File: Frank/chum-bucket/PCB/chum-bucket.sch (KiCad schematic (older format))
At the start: 3 parts

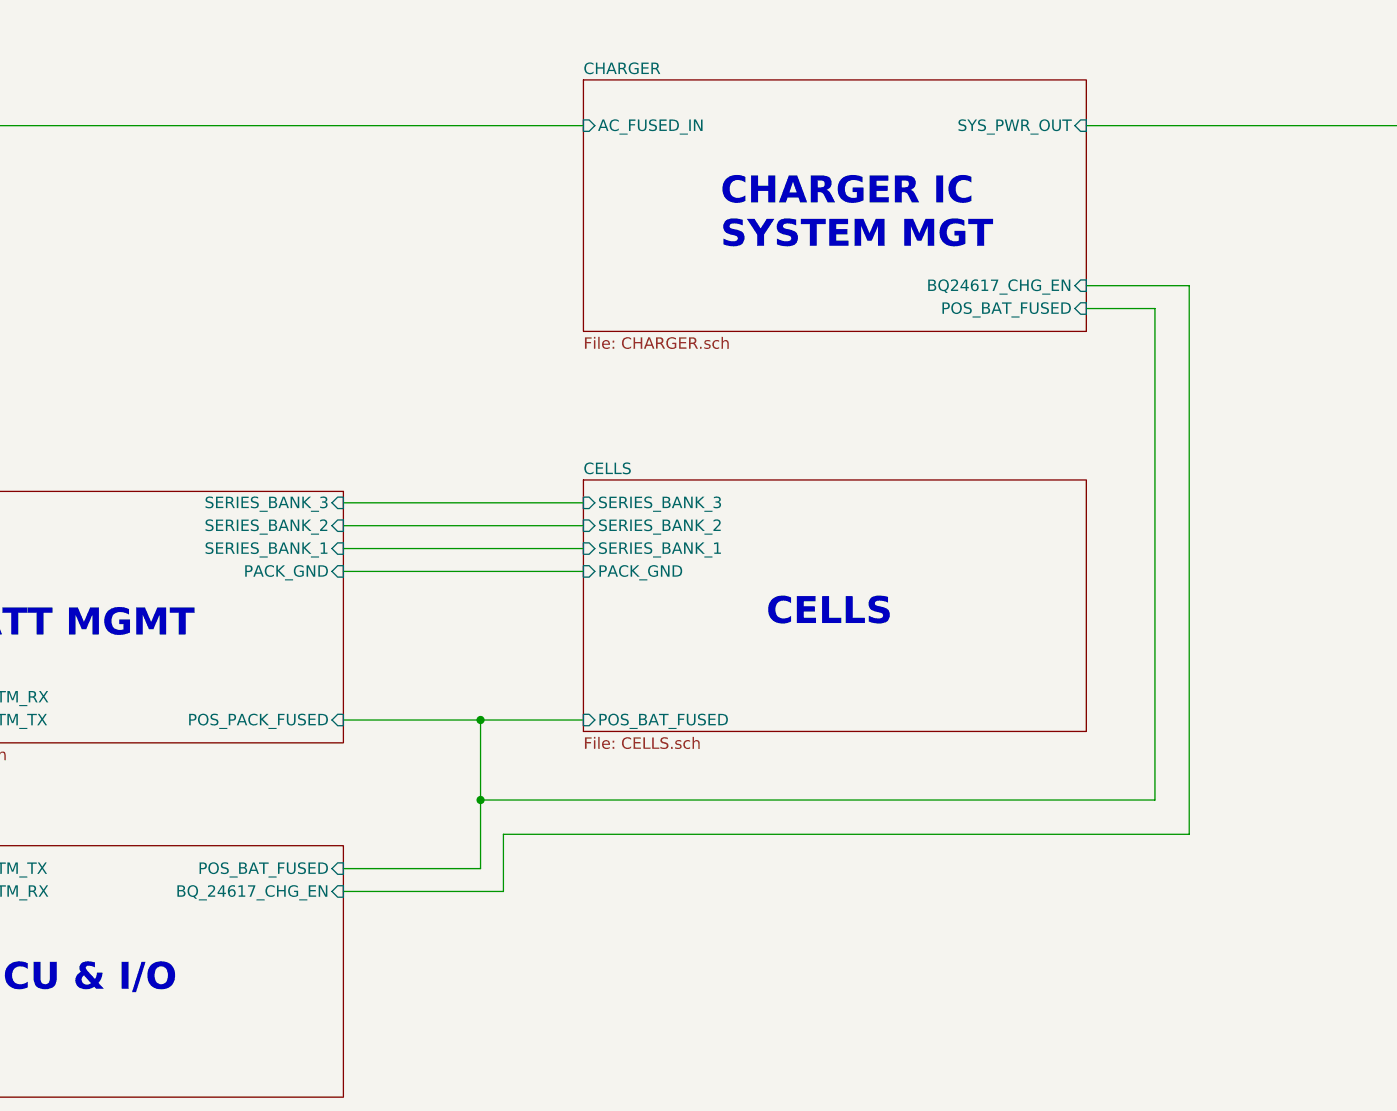
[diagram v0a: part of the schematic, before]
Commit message: minor schematic update + inrush sim
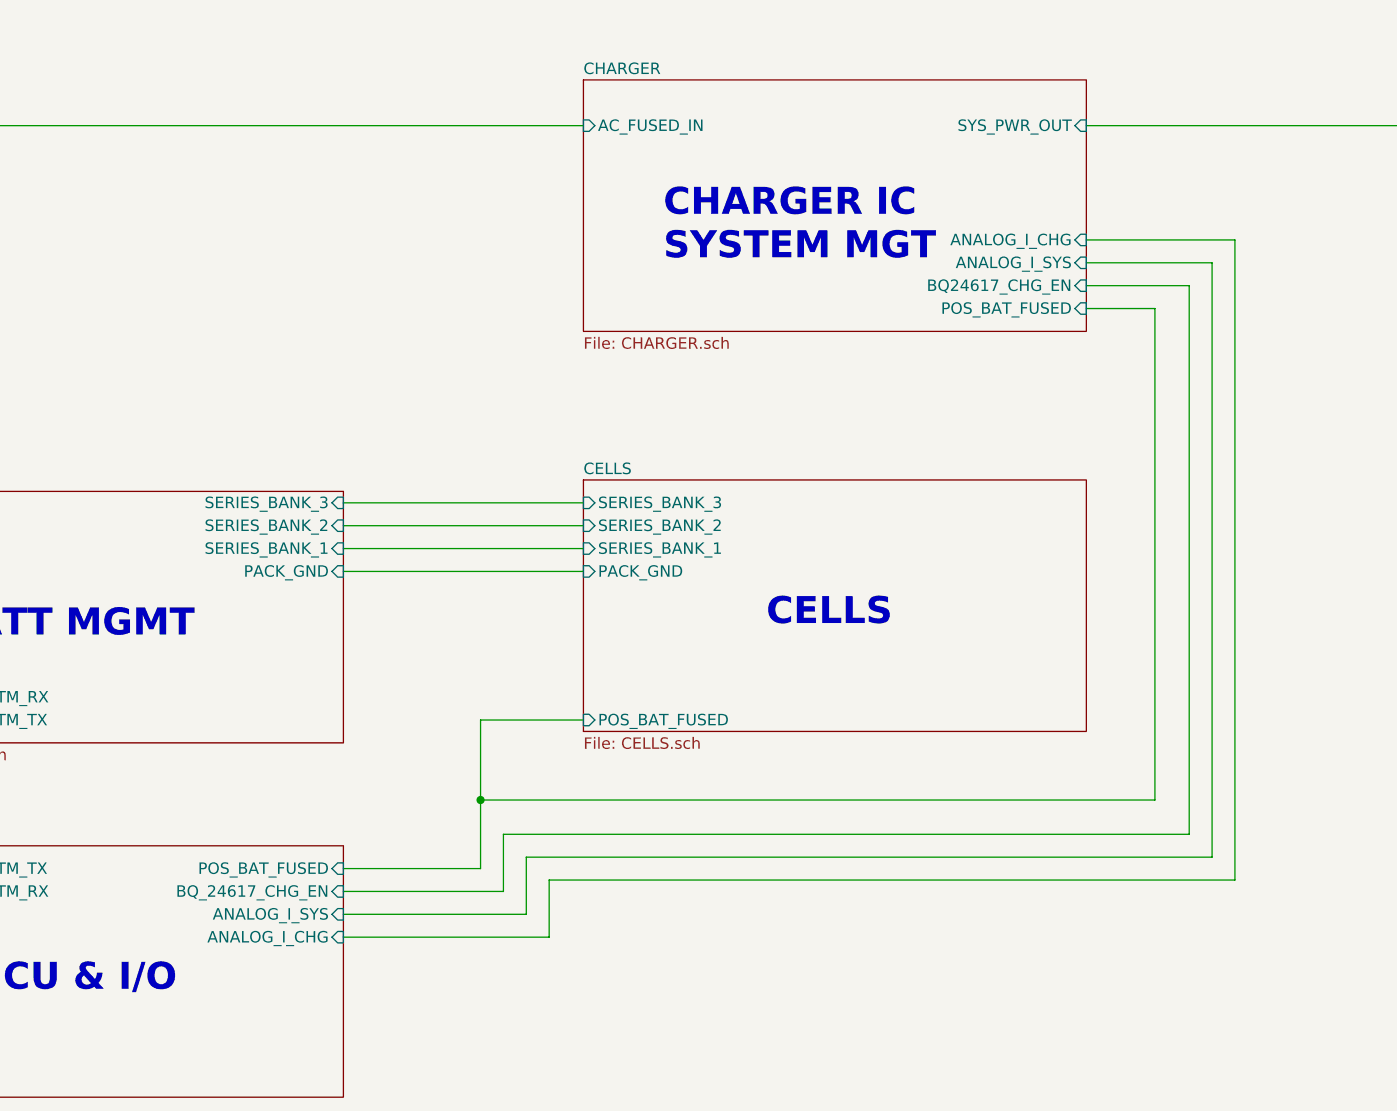
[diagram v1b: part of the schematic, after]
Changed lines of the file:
@@
 F6 "UART_BQ79606_STM_TX" I L 1550 5800 50
 F7 "UART_BQ79606_STM_RX" I L 1550 5900 50
+F8 "ANALOG_I_SYS" I R 3750 6000 50
+F9 "ANALOG_I_CHG" I R 3750 6100 50
 $EndSheet
 Text Notes 5600 4750 0    118  ~ 24
@@
 F6 "SERIES_BANK_3" I L 4800 4200 50
 $EndSheet
-Text Notes 5400 3100 0    118  ~ 24
+Text Notes 5150 3150 0    118  ~ 24
 CHARGER IC\nSYSTEM MGT
 $Sheet
@@
 F4 "SYS_PWR_OUT" I R 7000 2550 50
 F5 "POS_BAT_FUSED" I R 7000 3350 50
+F6 "ANALOG_I_SYS" I R 7000 3150 50
+F7 "ANALOG_I_CHG" I R 7000 3050 50
 $EndSheet
 $Sheet
@@
 F2 "~BQ79606_FAULT" I L 1550 4950 50
 F3 "BQ79606_WAKE" I L 1550 4850 50
-F4 "POS_PACK_FUSED" I R 3750 5150 50
-F5 "SERIES_BANK_3" I R 3750 4200 50
-F6 "SERIES_BANK_2" I R 3750 4300 50
-F7 "SERIES_BANK_1" I R 3750 4400 50
-F8 "PACK_GND" I R 3750 4500 50
-F9 "UART_BQ79606_STM_RX" I L 1550 5050 50
-F10 "UART_BQ79606_STM_TX" I L 1550 5150 50
+F4 "SERIES_BANK_3" I R 3750 4200 50
+F5 "SERIES_BANK_2" I R 3750 4300 50
+F6 "SERIES_BANK_1" I R 3750 4400 50
+F7 "PACK_GND" I R 3750 4500 50
+F8 "UART_BQ79606_STM_RX" I L 1550 5050 50
+F9 "UART_BQ79606_STM_TX" I L 1550 5150 50
 $EndSheet
 Text Notes 3100 4800 2    118  ~ 24
@@
 	4350 5800 4350 5500
 Wire Wire Line
-	3750 5150 4350 5150
-Wire Wire Line
 	4350 5500 4350 5150
 Connection ~ 4350 5500
-Connection ~ 4350 5150
 Wire Wire Line
 	4350 5150 4800 5150
@@
 Wire Wire Line
 	7450 3250 7000 3250
+Wire Wire Line
+	3750 6000 4550 6000
+Wire Wire Line
+	4550 6000 4550 5750
+Wire Wire Line
+	4550 5750 7550 5750
+Wire Wire Line
+	7550 5750 7550 3150
+Wire Wire Line
+	7550 3150 7000 3150
+Wire Wire Line
+	3750 6100 4650 6100
+Wire Wire Line
+	4650 6100 4650 5850
+Wire Wire Line
+	4650 5850 7650 5850
+Wire Wire Line
+	7650 5850 7650 3050
+Wire Wire Line
+	7650 3050 7000 3050
 $EndSCHEMATC

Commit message: Weekends work. Final component selection then ready for review :)
huge oof
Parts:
- removed F?: Fuse, symbol Device:Fuse
- removed J?: XT-30 RA, symbol Connector_Generic:Conn_01x02
- added J?: WPT_CONN, symbol Connector_Generic:Conn_01x02
- added J?: SYS_PWR, symbol Connector_Generic:Conn_01x02
- added J?: ESC_PWR, symbol Connector_Generic:Conn_01x02
- J?: value Conn_01x02 -> AC_ADPTR
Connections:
- net CHARGER/AC_FUSED_IN: now also J?.2 (Pin_2), J?.2 (Pin_2)
- net GND: now also J?.1 (Pin_1), J?.1 (Pin_1), J?.1 (Pin_1)
- new net SYS_MGMT/ESC_PWR_OUT: J?.2 (Pin_2)
- new net SYS_MGMT/SYS_PWR_OUT_PROT: J?.2 (Pin_2)
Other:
- note added: "- 1kW peak power delievery\n- e-fused I/O for decreased footprint\n- Power telemetry delievered via CAN"
- note added: "- 3s8p Lithium cell holders\n- 2A Balancing Current\n- 8A cell charger"
- note added: "CHARGER"
- note added: "Highly Integrated, Small Footprint, Managed Lithium Battery"
- note added: "No need to fuse due to use of \nconventionial and e-fuses downstream"
- note added: "SYS MGMT +\nOUTPUT PROT"
- note removed: "- 3s8p Lithium cell holder\n- Blah Blah\n- Item 3\n- Item 4"
- note removed: "- Item 1\n- Item 2\n- Item 3\n- Item 4"
- note removed: "CHARGER IC\nSYSTEM MGT"
- note removed: "Highly Integrated, Small Footprint, Protected Lithium Battery"
- moved on the sheet: J?

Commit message: batt-management sheet updates
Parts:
- added C?: 10nF, symbol Device:C_Small
- added D?: SMBJ26A, Diode_SMD:D_SMB, symbol Device:D_TVS
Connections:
- net CHARGER/AC_FUSED_IN: now also C?.1, D?.1 (A1)
- net GND: now also C?.2, D?.2 (A2)
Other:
- note added: "- 1kW peak power delievery\n- e-fused I/O for decreased footprint\n- Power telemetry broadcasted via CAN"
- note added: "To do: \n- add voltage monitoring for output busses\n- add current monitoring for ESC bus (hall effect sensor?)"
- note removed: "- 1kW peak power delievery\n- e-fused I/O for decreased footprint\n- Power telemetry delievered via CAN"
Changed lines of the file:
@@
 - 3s8p Lithium cell holders\n- 2A Balancing Current\n- 8A cell charger
 Text Notes 6150 1550 0    39   ~ 0
-- 1kW peak power delievery\n- e-fused I/O for decreased footprint\n- Power telemetry delievered via CAN
+- 1kW peak power delievery\n- e-fused I/O for decreased footprint\n- Power telemetry broadcasted via CAN
 Text Notes 7900 3200 0    118  ~ 24
 SYS MGMT +\nOUTPUT PROT
@@
 	-1   0    0    1
 $EndComp
-Text Notes 1400 2100 0    50   ~ 0
+Text Notes 1500 2450 0    50   ~ 0
 No need to fuse due to use of \nconventionial and e-fuses downstream
 Wire Wire Line
@@
 	6850 3350 7550 3350
 Connection ~ 1450 2550
-Wire Wire Line
-	1450 2550 2850 2550
 Wire Wire Line
 	4150 3900 2850 3900
@@
 F10 "ESC_PWR_EN" I R 6350 4150 50
 $EndSheet
+$Comp
+L Device:D_TVS D?
+U 1 1 5EFB8FC1
+P 1900 2850
+AR Path="/5F507ADF/5EFB8FC1" Ref="D?"  Part="1"
+AR Path="/5EFB8FC1" Ref="D?"  Part="1"
+F 0 "D?" V 1854 2929 50  0000 L CNN
+F 1 "SMBJ26A" V 1945 2929 50  0000 L CNN
+F 2 "Diode_SMD:D_SMB" H 1900 2850 50  0001 C CNN
+F 3 "https://www.vishay.com/docs/88392/smbj.pdf" H 1900 2850 50  0001 C CNN
+F 4 "SMBJ26A-E3/5BGITR-ND" V 1900 2850 50  0001 C CNN "Digikey"
+	1    1900 2850
+	0    -1   1    0
+$EndComp
+$Comp
+L power:GND #PWR?
+U 1 1 5EFB8FC7
+P 1900 3100
+AR Path="/5F507ADF/5EFB8FC7" Ref="#PWR?"  Part="1"
+AR Path="/5EFB8FC7" Ref="#PWR?"  Part="1"
+F 0 "#PWR?" H 1900 2850 50  0001 C CNN
+F 1 "GND" H 1905 2927 50  0000 C CNN
+F 2 "" H 1900 3100 50  0001 C CNN
+F 3 "" H 1900 3100 50  0001 C CNN
+	1    1900 3100
+	1    0    0    -1
+$EndComp
+Wire Wire Line
+	1900 3100 1900 3000
+$Comp
+L Device:C_Small C?
+U 1 1 5EFB8FCE
+P 2100 2850
+AR Path="/5F507ADF/5EFB8FCE" Ref="C?"  Part="1"
+AR Path="/5EFB8FCE" Ref="C?"  Part="1"
+F 0 "C?" H 2192 2896 50  0000 L CNN
+F 1 "10nF" H 2192 2805 50  0000 L CNN
+F 2 "" H 2100 2850 50  0001 C CNN
+F 3 "~" H 2100 2850 50  0001 C CNN
+	1    2100 2850
+	1    0    0    -1
+$EndComp
+$Comp
+L power:GND #PWR?
+U 1 1 5EFB8FD4
+P 2100 3100
+AR Path="/5F507ADF/5EFB8FD4" Ref="#PWR?"  Part="1"
+AR Path="/5EFB8FD4" Ref="#PWR?"  Part="1"
+F 0 "#PWR?" H 2100 2850 50  0001 C CNN
+F 1 "GND" H 2105 2927 50  0000 C CNN
+F 2 "" H 2100 3100 50  0001 C CNN
+F 3 "" H 2100 3100 50  0001 C CNN
+	1    2100 3100
+	1    0    0    -1
+$EndComp
+Wire Wire Line
+	2100 3100 2100 2950
+Wire Wire Line
+	1900 2700 1900 2550
+Wire Wire Line
+	2100 2750 2100 2550
+Connection ~ 1900 2550
+Connection ~ 2100 2550
+Wire Wire Line
+	2100 2550 2850 2550
+Wire Wire Line
+	1450 2550 1900 2550
+Wire Wire Line
+	1900 2550 2100 2550
+Text Notes 7650 4250 0    50   Italic 0
+To do: \n- add voltage monitoring for output busses\n- add current monitoring for ESC bus (hall effect sensor?)
 $EndSCHEMATC

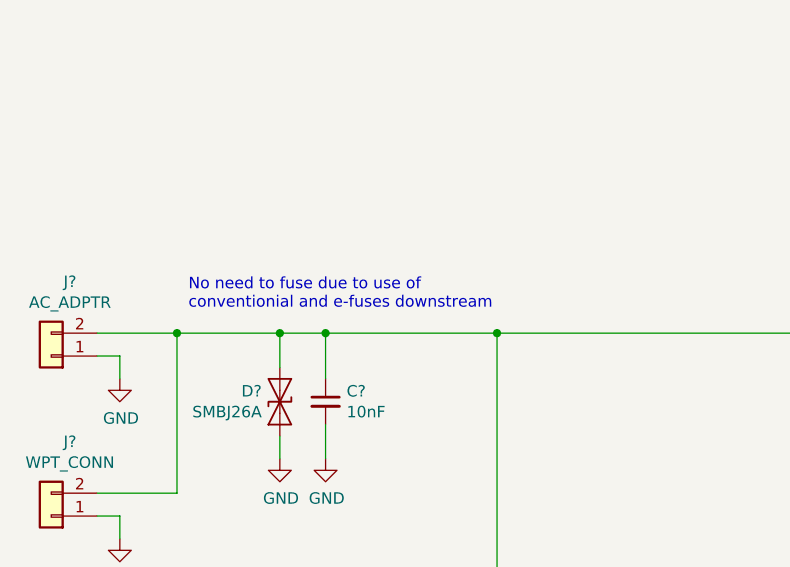
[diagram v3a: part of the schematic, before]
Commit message: Minor schematic organization changes
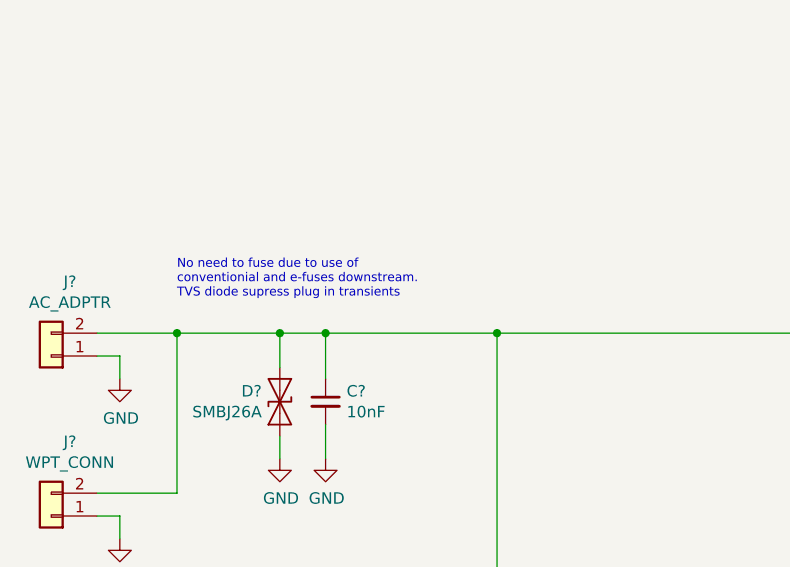
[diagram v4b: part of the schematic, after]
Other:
- note added: "No need to fuse due to use of \nconventionial and e-fuses downstream.\nTVS diode supress plug in transients"
- note removed: "No need to fuse due to use of \nconventionial and e-fuses downstream"
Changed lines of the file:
@@
 	-1   0    0    1
 $EndComp
-Text Notes 1500 2450 0    50   ~ 0
-No need to fuse due to use of \nconventionial and e-fuses downstream
+Text Notes 1450 2400 0    39   ~ 0
+No need to fuse due to use of \nconventionial and e-fuses downstream.\nTVS diode supress plug in transients
 Wire Wire Line
 	1100 3250 1450 3250

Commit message: for review at 2pm
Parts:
- added C?: 470uF, symbol Device:CP_Small
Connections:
- net GND: now also C?.2
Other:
- note added: "- 3s8p Lithium cell holders\n- 1A Balancing Current\n- 8A cell charging"
- note removed: "- 3s8p Lithium cell holders\n- 2A Balancing Current\n- 8A cell charger"
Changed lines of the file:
@@
 Highly Integrated, Small Footprint, Managed Lithium Battery
 Text Notes 4900 1550 0    39   ~ 0
-- 3s8p Lithium cell holders\n- 2A Balancing Current\n- 8A cell charger
+- 3s8p Lithium cell holders\n- 1A Balancing Current\n- 8A cell charging
 Text Notes 6150 1550 0    39   ~ 0
 - 1kW peak power delievery\n- e-fused I/O for decreased footprint\n- Power telemetry broadcasted via CAN
@@
 Text Notes 7650 4250 0    50   Italic 0
 To do: \n- add voltage monitoring for output busses\n- add current monitoring for ESC bus (hall effect sensor?)
+$Comp
+L power:GND #PWR?
+U 1 1 5EF84B97
+P 2450 3100
+AR Path="/5F507ADF/5EF84B97" Ref="#PWR?"  Part="1"
+AR Path="/5EF84B97" Ref="#PWR?"  Part="1"
+F 0 "#PWR?" H 2450 2850 50  0001 C CNN
+F 1 "GND" H 2455 2927 50  0000 C CNN
+F 2 "" H 2450 3100 50  0001 C CNN
+F 3 "" H 2450 3100 50  0001 C CNN
+	1    2450 3100
+	1    0    0    -1
+$EndComp
+Wire Wire Line
+	2450 3100 2450 2950
+Wire Wire Line
+	2450 2750 2450 2550
+$Comp
+L Device:CP_Small C?
+U 1 1 5EF85CBA
+P 2450 2850
+F 0 "C?" H 2538 2896 50  0000 L CNN
+F 1 "470uF" H 2538 2805 50  0000 L CNN
+F 2 "" H 2450 2850 50  0001 C CNN
+F 3 "~" H 2450 2850 50  0001 C CNN
+F 4 "P15451TR-ND" H 2450 2850 50  0001 C CNN "Digikey"
+	1    2450 2850
+	1    0    0    -1
+$EndComp
 $EndSCHEMATC
